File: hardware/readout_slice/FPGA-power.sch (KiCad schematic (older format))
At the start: 61 parts

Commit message: auto push run at Wed Apr 21 10:59:57 EDT 2021
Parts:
- removed C? (x2): .10u, symbol Device:C_Small
- added C? (x2): 1u, symbol Device:C_Small
- added C? (x4): C, symbol Device:C_Small
- added C? (x2): .10u, symbol Device:C_Small
- added J?: mini-fit jr, symbol Connector_Generic:Conn_02x02_Counter_Clockwise
- added R? (x5): R, symbol Device:R_Small
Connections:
- net labels added: Vreg
- wire segments 493 -> 515
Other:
- note added: "Enables?"
- note added: "to LED"
- note added: "to where?"
- note added: "voltage\n"
- note removed: "finish this schematic\n"
- moved on the sheet: C?, L?, R?, U?

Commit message: auto push run at Wed Apr 21 11:17:43 EDT 2021
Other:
- note added: "1.2v to 5V to 1.2A"
- note added: "1.2v to 5V to 4A"
- note added: "dropout to .2A"
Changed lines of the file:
@@
 	2700 7100 2700 7000
 Connection ~ 2800 7100
+Text Notes 5750 3850 0    50   ~ 10
+1.2v to 5V to 4A
+Text Notes 5800 4900 0    50   ~ 10
+1.2v to 5V to 4A
+Text Notes 5100 5550 0    50   ~ 10
+1.2v to 5V to 1.2A
+Text Notes 4900 6150 0    50   ~ 10
+1.2v to 5V to 1.2A
+Text Notes 3850 6800 0    50   ~ 10
+dropout to .2A
 $EndSCHEMATC

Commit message: auto push run at Wed Apr 21 11:22:25 EDT 2021
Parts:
- added SW?: SW_SPDT, symbol Switch:SW_SPDT
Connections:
- wire segments 515 -> 519
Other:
- moved on the sheet: C?, J?, U?C

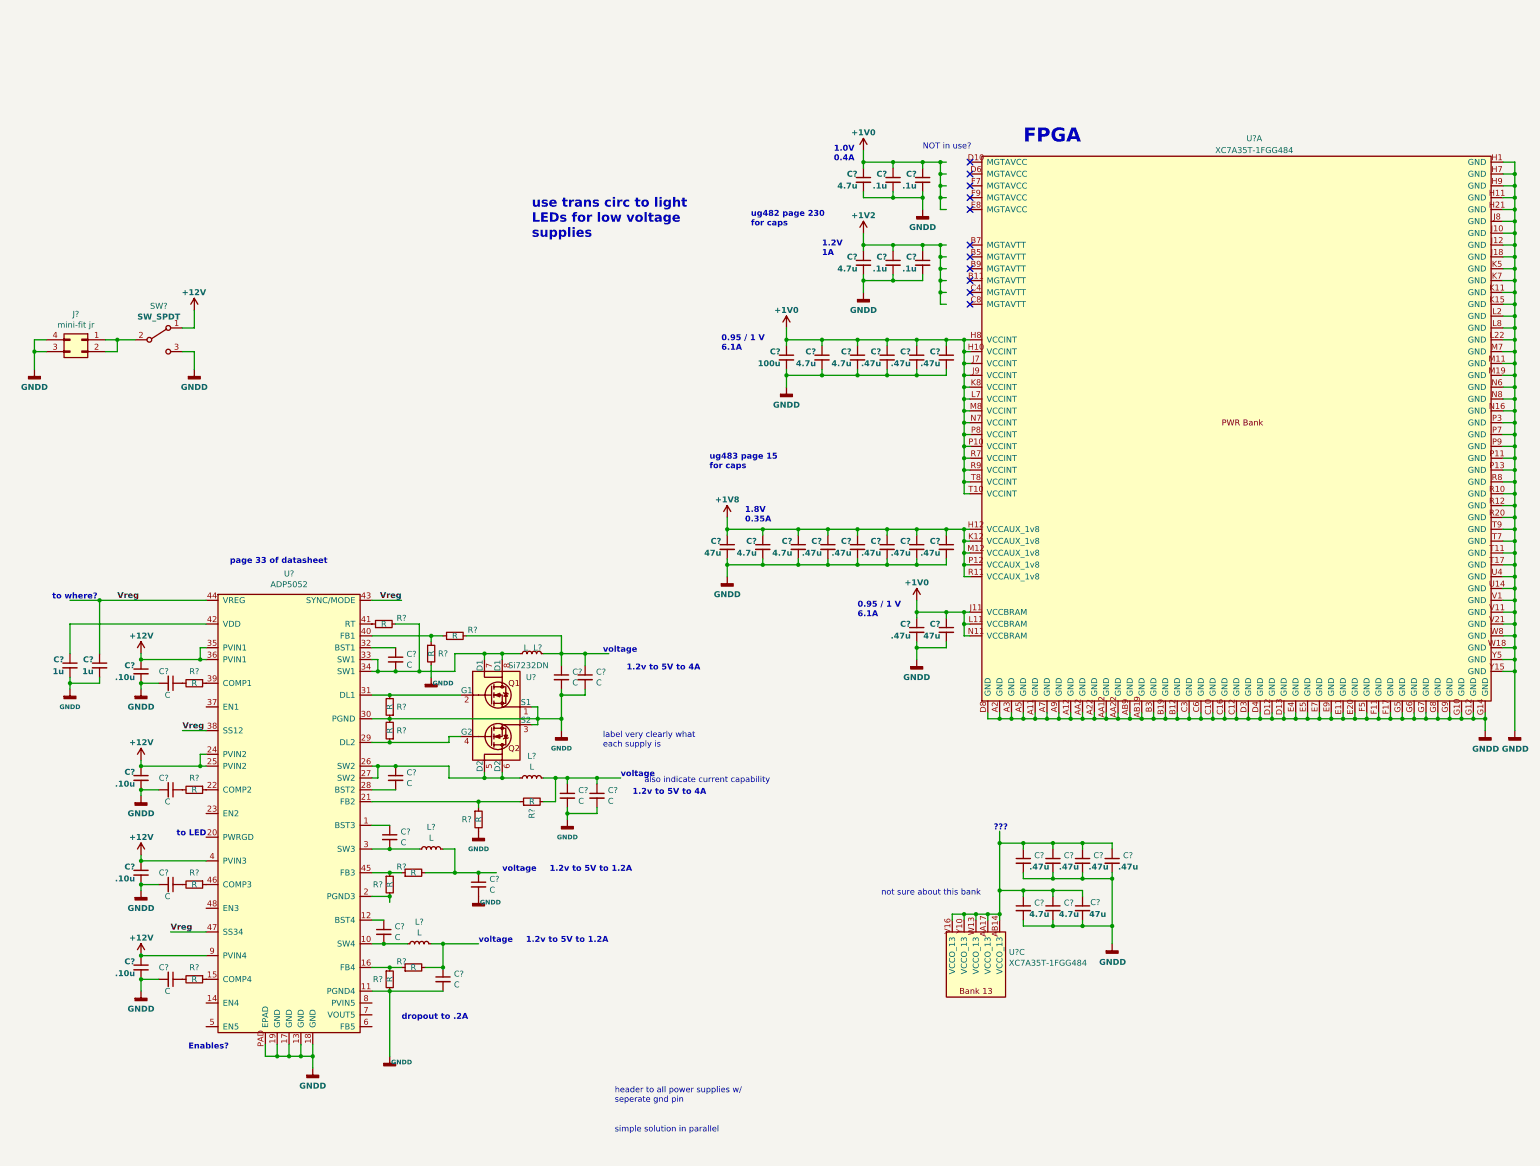
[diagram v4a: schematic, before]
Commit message: removed zx2, added sfp for serdes from dan's vice board
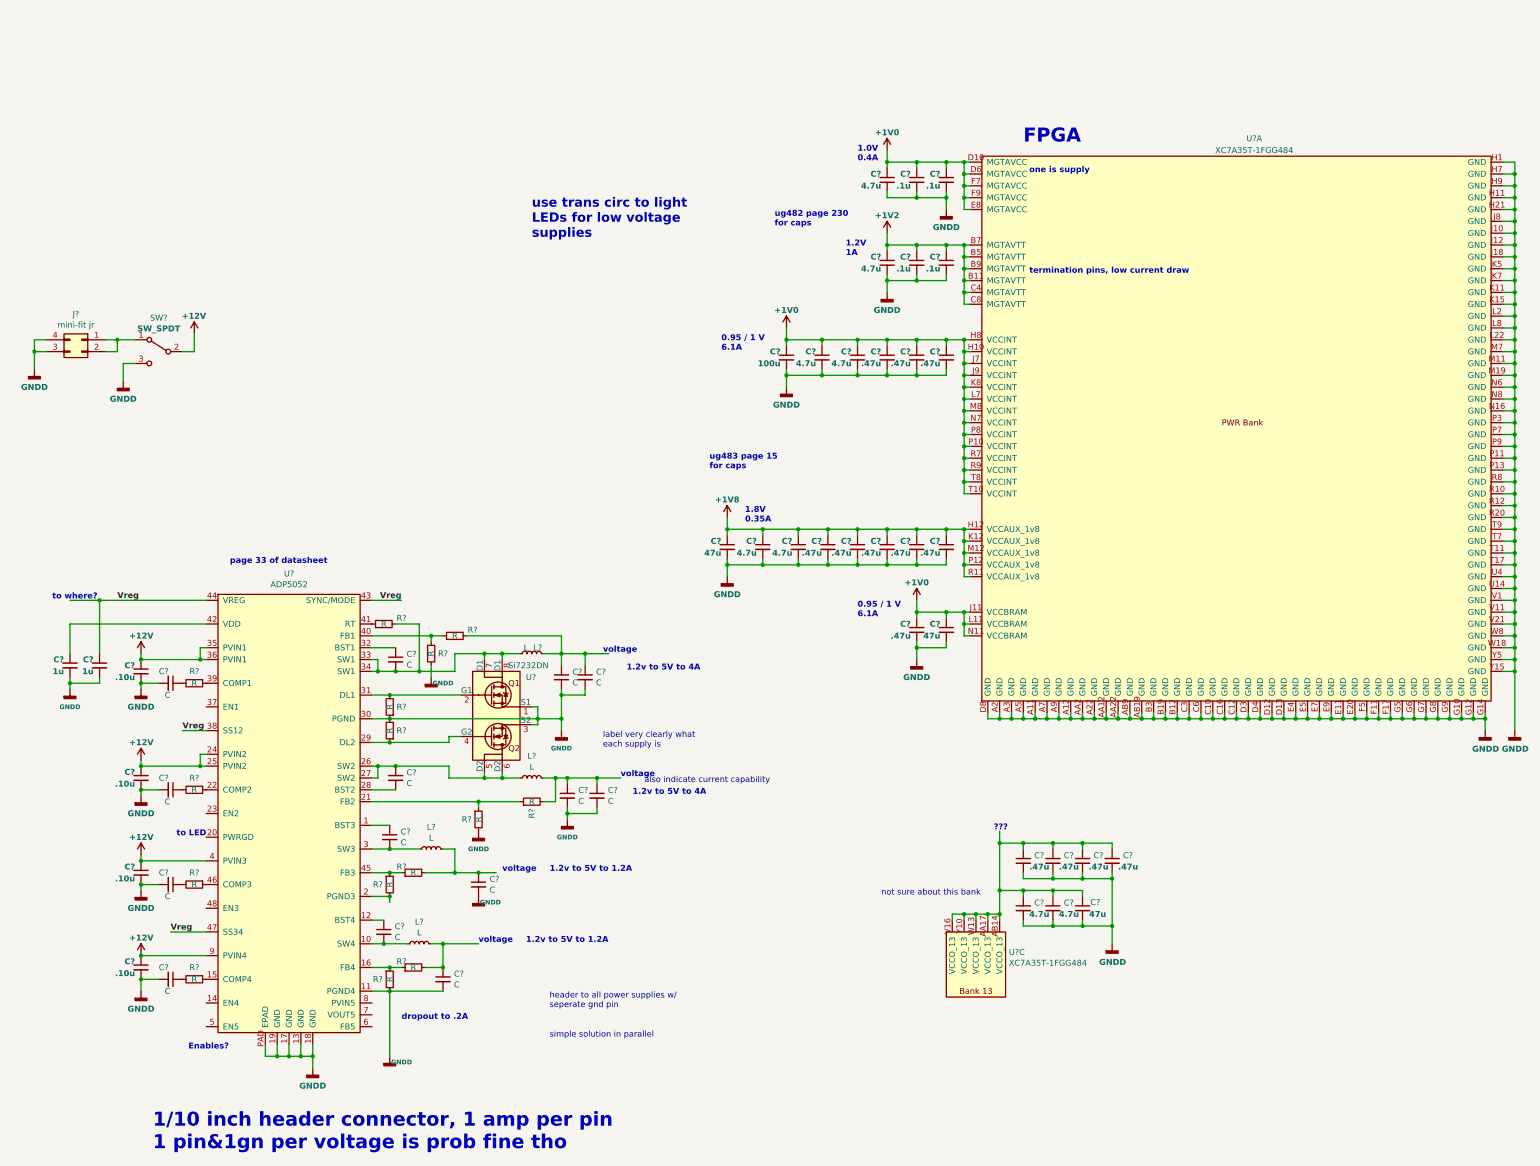
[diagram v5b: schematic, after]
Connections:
- no-connect marks 11 -> 0
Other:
- note added: "1/10 inch header connector, 1 amp per pin\n1 pin&1gn per voltage is prob fine tho\n"
- note added: "one is supply\n"
- note added: "termination pins, low current draw\n"
- note removed: "NOT in use?"
- moved on the sheet: C?, SW?

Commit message: auto push run at Wed Apr 28 10:36:58 EDT 2021
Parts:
- added C? (x2): 2.2u, symbol Device:C_Small
- added C? (x2): 1u, symbol Device:C_Small
- added C? (x2): .1u, symbol Device:C_Small
- added U?: TPS72010, symbol readout:TPS72
- added U?: TPS72012, symbol readout:TPS72
- added U? (x2): VccMGTAVcc, symbol readout:VccMGTAVcc
- added U? (x2): VccMGTAVtt, symbol readout:VccMGTAVtt
- added U? (x4): 2.2V, symbol readout:2.2V
- added U?: VccAux, symbol readout:VccAux
- added U?: VccInt, symbol readout:VccInt
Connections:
- net +1V8 is gone; now on net VCC: C?.1, C?.1, C?.1, C?.1, C?.1, C?.1, C?.1, C?.1, U?.H12 (VCCAUX_1v8), U?.K12 (VCCAUX_1v8), U?.M12 (VCCAUX_1v8), U?.P12 (VCCAUX_1v8), U?.R11 (VCCAUX_1v8)
- net +1V0: no longer C?.1, C?.1, C?.1, C?.1, C?.1, C?.1, C?.1, C?.1, C?.1, U?.D10 (MGTAVCC), U?.D6 (MGTAVCC), U?.E8 (MGTAVCC), U?.F7 (MGTAVCC), U?.F9 (MGTAVCC), U?.H10 (VCCINT), U?.H8 (VCCINT), U?.J7 (VCCINT), U?.J9 (VCCINT), U?.K8 (VCCINT), U?.L7 (VCCINT), U?.M8 (VCCINT), U?.N7 (VCCINT), U?.P10 (VCCINT), U?.P8 (VCCINT), U?.R7 (VCCINT), U?.R9 (VCCINT), U?.T10 (VCCINT), U?.T8 (VCCINT)
- net +1V2 renamed VCC
- net VCC: now also C?.1, C?.1, C?.1, C?.1, C?.1, C?.1, C?.1, C?.1, C?.1, U?.D10 (MGTAVCC), U?.D6 (MGTAVCC), U?.E8 (MGTAVCC), U?.F7 (MGTAVCC), U?.F9 (MGTAVCC), U?.H10 (VCCINT), U?.H8 (VCCINT), U?.J7 (VCCINT), U?.J9 (VCCINT), U?.K8 (VCCINT), U?.L7 (VCCINT), U?.M8 (VCCINT), U?.N7 (VCCINT), U?.P10 (VCCINT), U?.P8 (VCCINT), U?.R7 (VCCINT), U?.R9 (VCCINT), U?.T10 (VCCINT), U?.T8 (VCCINT), C?.1, C?.1, C?.1, C?.1, C?.1, C?.1, U?.1 (Out), U?.1 (Out), U?.1 (VCC), U?.1 (VCC), U?.1 (VCC), U?.1 (VCC), U?.1 (VCC), U?.1 (VCC), U?.1 (VCC), U?.1 (VCC), U?.1 (VCC), U?.1 (VCC), U?.4 (Bias), U?.4 (Bias), U?.6 (In), U?.6 (In)
- new net GNDA: C?.2, C?.2, C?.2, C?.2, C?.2, C?.2, U?.5 (GND), U?.5 (GND), U?.pad, U?.pad

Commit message: working on power
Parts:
- removed C? (x4): .10u, symbol Device:C_Small
- removed C? (x14): C, symbol Device:C_Small
- removed C? (x2): 1u, symbol Device:C_Small
- removed L? (x4): L, symbol Device:L_Small
- removed R? (x15): R, symbol Device:R_Small
- removed U?: ADP5052, symbol readout:ADP5052
- removed U?: Si7232DN, symbol readout:Si7232DN
- added C?: .1u, symbol Device:C_Small
- added R? (x3): 10k, symbol Device:R
- added U?: LM3880, Package_TO_SOT_SMD:SOT-23-6, symbol Power_Supervisor:LM3880
- added U?: 2.2V, symbol readout:2.2V
- added U?: 3.6V, symbol readout:3.6V
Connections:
- net GNDA: now also C?.1, U?.2 (GND)
- net VCC: now also R?.1, R?.1, R?.1, U?.1 (VCC), U?.1 (VCC)
- net PWRUP_1: now reaches U?.3 (En)
- net PWRUP_1: now also R?.2, U?.6 (FLAG1)
- net PWRUP_2: now reaches U?.3 (En)
- net PWRUP_2: now also R?.2, U?.5 (FLAG2)
- new net +5V: C?.2, U?.1 (VCC)
- new net LV_PWR_EN: U?.3 (EN)
- new net PWRUP_3: R?.2, U?.4 (FLAG3)
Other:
- note added: "Control, 2v5 good (60ms/60ms/60ms)\n1) VccINT, VccBRAM, VccMGTAVCC\n2) VccAUX, VCCMGTAVtt\n3) FPGA banks"
- note added: "check if linear regulator"
- note removed: "1.2v to 5V to 1.2A"
- note removed: "1.2v to 5V to 4A"
- note removed: "Enables?"
- note removed: "also indicate current capability"
- note removed: "dropout to .2A"
- note removed: "header to all power supplies w/\nseperate gnd pin"
- note removed: "label very clearly what\neach supply is"
- note removed: "page 33 of datasheet"
- note removed: "simple solution in parallel"
- note removed: "to LED"
- note removed: "to where?"
- note removed: "voltage\n"
- moved on the sheet: C?, J?, SW?, U?

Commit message: more power
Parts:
- removed C? (x3): .1u, symbol Device:C_Small
- removed C? (x2): 2.2u, symbol Device:C_Small
- removed C? (x2): 1u, symbol Device:C_Small
- removed J?: mini-fit jr, symbol Connector_Generic:Conn_02x02_Counter_Clockwise
- removed R? (x3): 10k, symbol Device:R
- removed SW?: SW_SPDT, symbol Switch:SW_SPDT
- removed U?: LM3880, Package_TO_SOT_SMD:SOT-23-6, symbol Power_Supervisor:LM3880
- removed U? (x5): 2.2V, symbol readout:2.2V
- removed U?: 3.6V, symbol readout:3.6V
- removed U?: TPS72010, symbol readout:TPS72
- removed U?: TPS72012, symbol readout:TPS72
- removed U?: VccMGTAVcc, symbol readout:VccMGTAVcc
- removed U?: VccMGTAVtt, symbol readout:VccMGTAVtt
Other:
- note removed: "1/10 inch header connector, 1 amp per pin\n1 pin&1gn per voltage is prob fine tho\n"
- note removed: "Control, 2v5 good (60ms/60ms/60ms)\n1) VccINT, VccBRAM, VccMGTAVCC\n2) VccAUX, VCCMGTAVtt\n3) FPGA banks"
- note removed: "use trans circ to light\nLEDs for low voltage\nsupplies"
- moved on the sheet: C?, U?A, U?C
